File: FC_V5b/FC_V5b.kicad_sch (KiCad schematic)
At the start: 78 parts, among them IC2 AZ1117CH-3.3TRG1, IC3 RV-3028-C7_32.768kHz_1ppm_TA_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, J1 Conn_01x02, J12 USB_C_Receptacle_USB2.0_16P, J16 DEBUG, J22 SWD Port, J3 Life Makes Lemonade, J4 Molex 503398-1892, J5 BM04B-SRSS-TB(LF)(SN), J6 Conn_Coaxial, J9 BM04B-SRSS-TB(LF)(SN), SW1 KMR2, SW2 KMR2, SW3 SW_Push_SPDT, U12 TCA9548ARGERQ1, U16 MCP9808T-E/MS, U30 E28-2G4M27S, U4 RFM98PW, U5 RFM9xBreakout, U7 LSM6DSOTR, U8 LSM303AGRTR

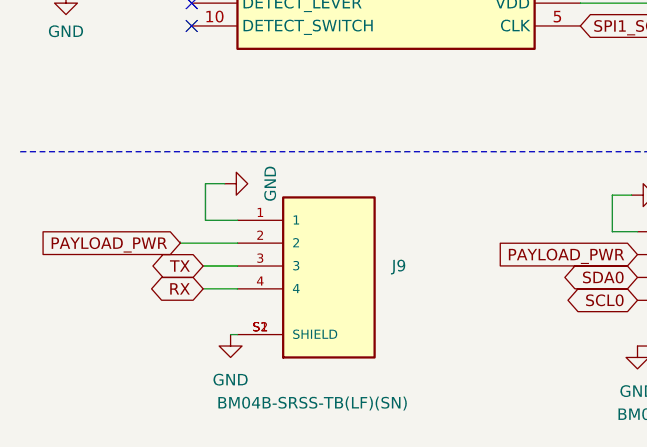
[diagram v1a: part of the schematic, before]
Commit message: Removed UART STEMMA
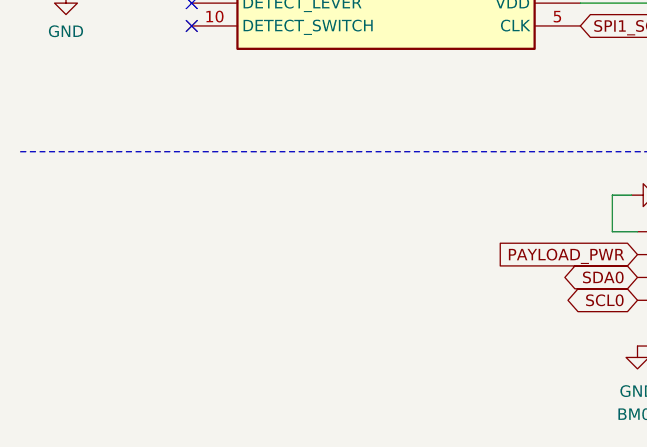
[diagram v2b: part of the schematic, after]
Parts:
- removed J9: BM04B-SRSS-TB(LF)(SN), FC_DEV_BOARD:JST_BM04B-SRSS-TB(LF)(SN), symbol BM04B-SRSS-TB_LF__SN_:BM04B-SRSS-TB(LF)(SN)

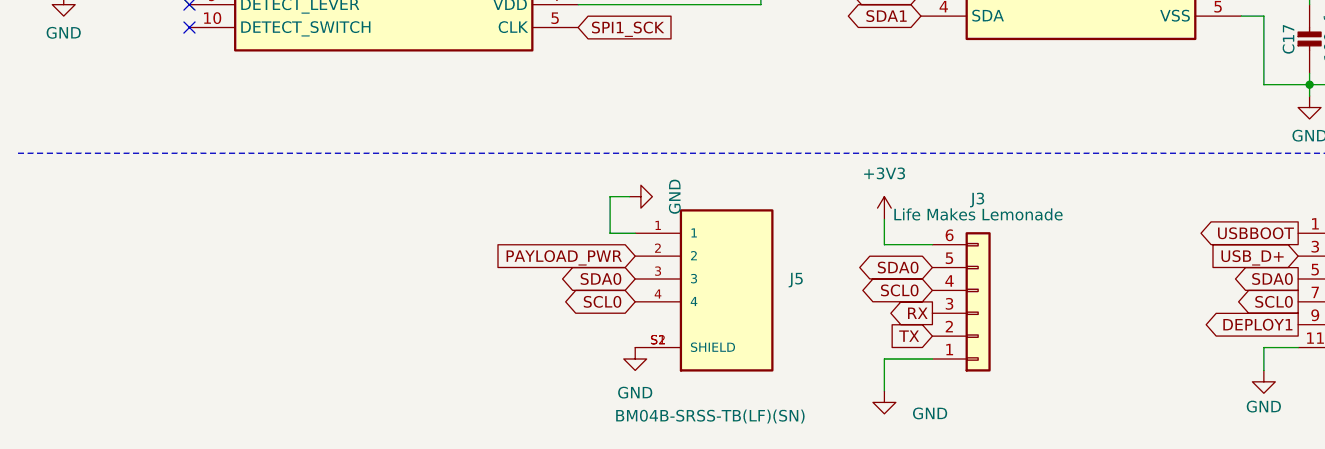
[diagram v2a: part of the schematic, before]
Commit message: Added a 12pos DF11 for Payload Connection
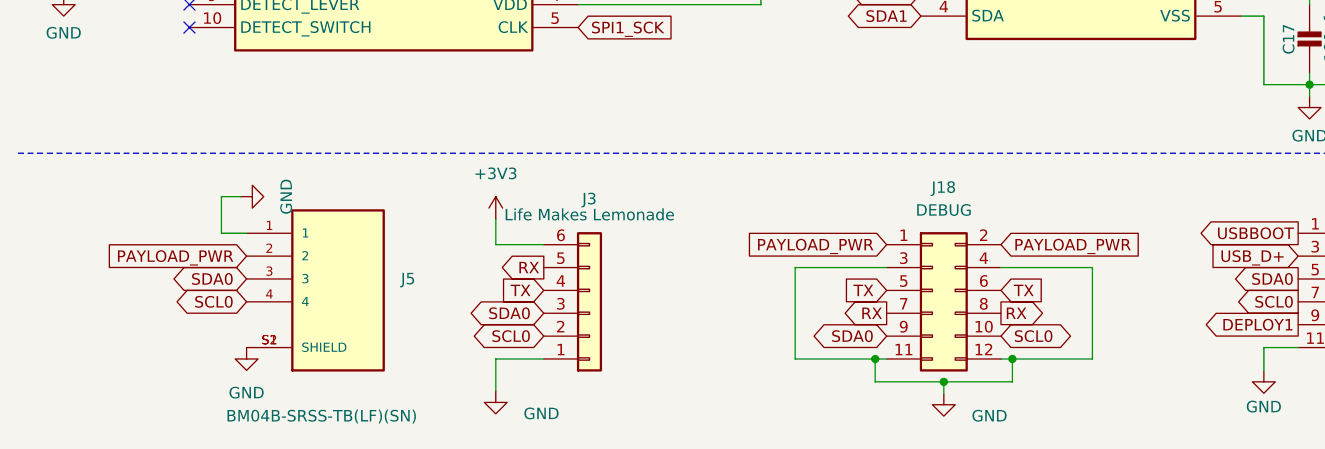
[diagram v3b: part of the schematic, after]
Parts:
- added J18: DEBUG, Connector_Hirose:Hirose_DF11-12DP-2DSA_2x06_P2.00mm_Vertical, symbol Connector_Generic:Conn_02x06_Odd_Even
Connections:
- net GND: now also J18.11 (Pin_11), J18.12 (Pin_12), J18.3 (Pin_3), J18.4 (Pin_4)
- net PAYLOAD_PWR: now also J18.1 (Pin_1), J18.2 (Pin_2)
- net RX: now also J3.5 (Pin_5), J18.7 (Pin_7), J18.8 (Pin_8); no longer J3.3 (Pin_3)
- net SCL0: now also J3.2 (Pin_2), J18.10 (Pin_10); no longer J3.4 (Pin_4)
- net SDA0: now also J3.3 (Pin_3), J18.9 (Pin_9); no longer J3.5 (Pin_5)
- net TX: now also J3.4 (Pin_4), J18.5 (Pin_5), J18.6 (Pin_6); no longer J3.2 (Pin_2)
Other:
- moved on the sheet: J3, J5

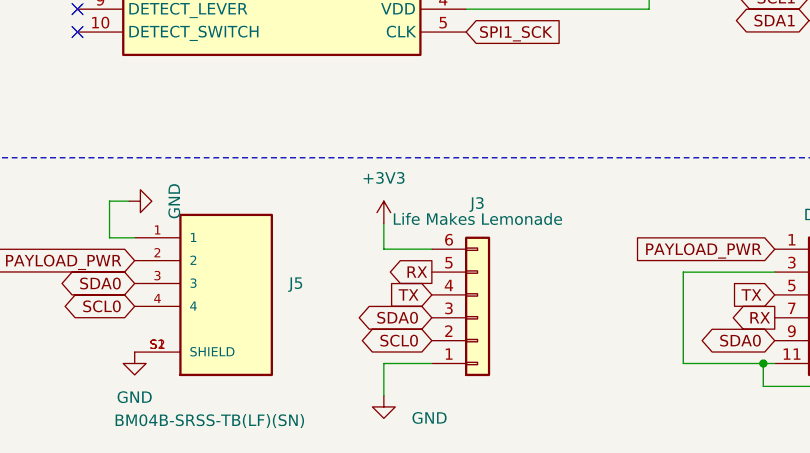
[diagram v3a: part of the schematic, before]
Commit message: Reduced TCA Solder Mask
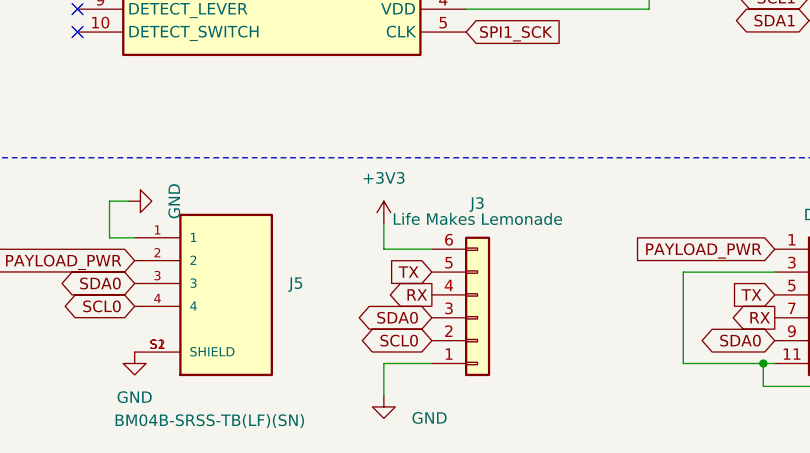
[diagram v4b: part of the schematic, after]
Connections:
- net RX: now also J3.4 (Pin_4); no longer J3.5 (Pin_5)
- net TX: now also J3.5 (Pin_5); no longer J3.4 (Pin_4)

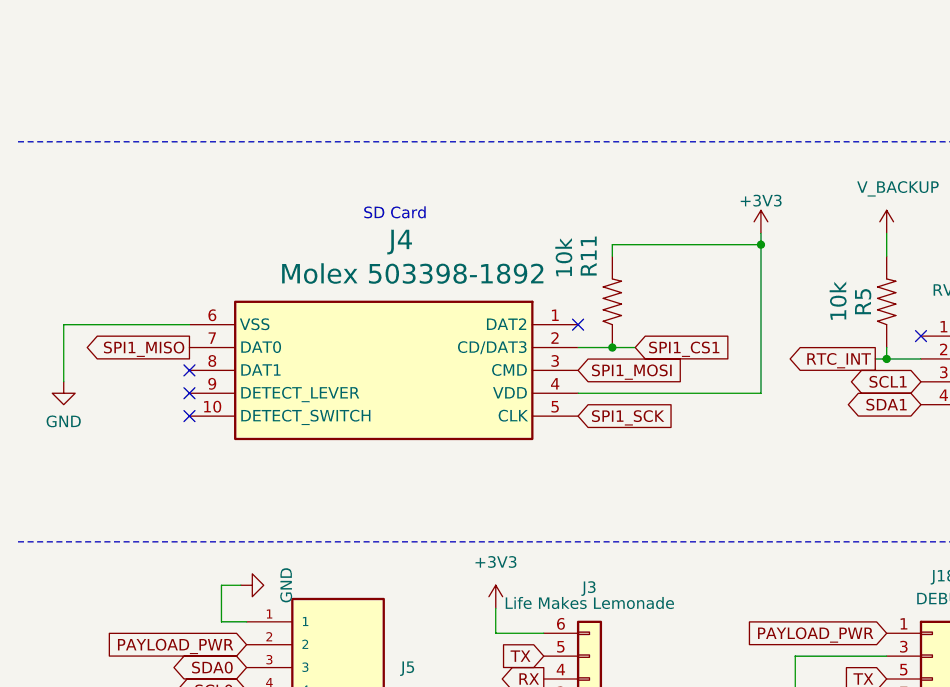
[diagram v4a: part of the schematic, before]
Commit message: Replaced SD Card Slot with ZSD NAND Chip
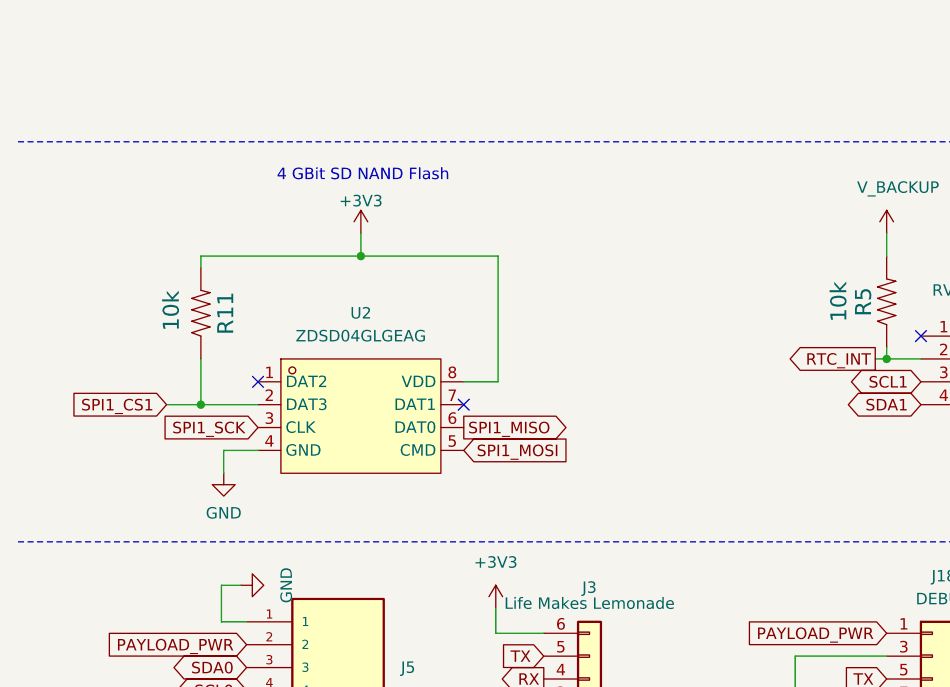
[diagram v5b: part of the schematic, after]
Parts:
- removed J4: Molex 503398-1892, 503398-1892-1, symbol Molex 503398-1892:503398-1892
- added U2: ZDSD04GLGEAG, easyeda2kicad:LGA-8_L8.0-W6.0-P1.27-TL-1, symbol easyeda2kicad:ZDSD04GLGEAG
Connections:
- net +3V3: now also U2.8 (VDD)
- net GND: now also U2.4 (GND)
- net SPI1_CS1: now also U2.2 (DAT3)
- net SPI1_MISO: now also U2.6 (DAT0)
- net SPI1_MOSI: now also U2.5 (CMD)
- net SPI1_SCK: now also U2.3 (CLK)
- no-connect marks 33 -> 31
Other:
- note added: "4 GBit SD NAND Flash"
- note removed: "SD Card"
- moved on the sheet: R11

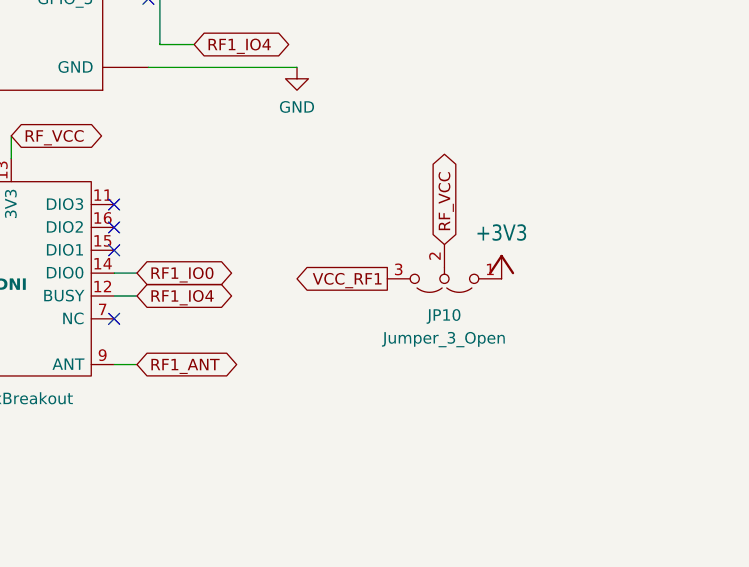
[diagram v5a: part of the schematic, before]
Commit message: Removed Unusued RF Power Selector
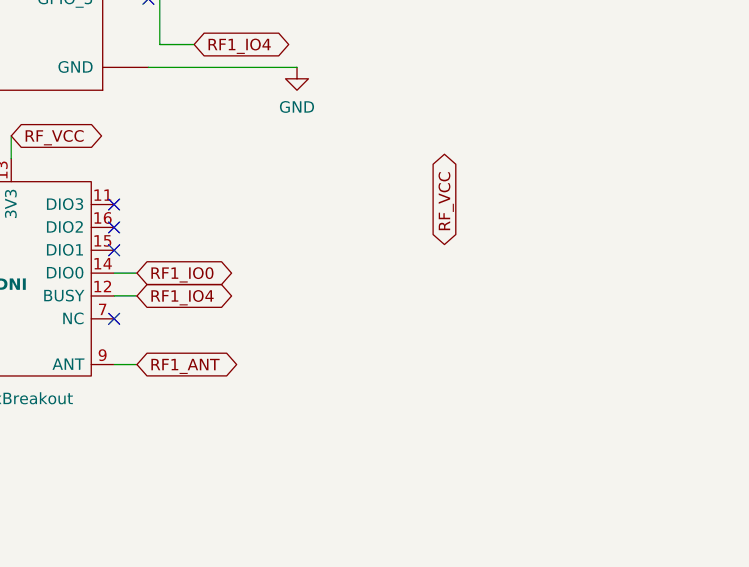
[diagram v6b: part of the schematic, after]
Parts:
- removed JP10: Jumper_3_Open, Jumper:SolderJumper-3_P1.3mm_Open_RoundedPad1.0x1.5mm_NumberLabels, symbol Jumper:Jumper_3_Open
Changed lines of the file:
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@@
 		)
 	)
-	(global_label "VCC_RF1"
-		(shape output)
-		(at 380.873 236.855 180)
-		(fields_autoplaced yes)
-		(effects
-			(font
-				(size 1.27 1.27)
-			)
-			(justify right)
-		)
-		(property "Intersheetrefs" "${INTERSHEET_REFS}"
-			(at 369.8029 236.855 0)
-			(effects
-				(font
-					(size 1.27 1.27)
-				)
-				(justify right)
-				(hide yes)
-			)
-		)
-	)
 	(symbol
 		(lib_id "mainboard:RESISTOR0603")
@@
 	)
 	(symbol
-		(lib_id "Adafruit ItsyBitsy RP2040-eagle-import:+3V3")
-		(at 393.573 234.315 0)
-		(unit 1)
-		(exclude_from_sim no)
-		(in_bom yes)
-		(on_board yes)
-		(dnp no)
-		(fields_autoplaced yes)
-		(property "Reference" "#+3V016"
-			(at 393.573 234.315 0)
-			(effects
-				(font
-					(size 1.27 1.27)
-				)
-				(hide yes)
-			)
-		)
-		(property "Value" "+3V3"
-			(at 393.573 231.775 0)
-			(effects
-				(font
-					(size 1.778 1.5113)
-				)
-			)
-		)
-		(property "Footprint" "Adafruit ItsyBitsy RP2040:"
-			(at 393.573 234.315 0)
-			(effects
-				(font
-					(size 1.27 1.27)
-				)
-				(hide yes)
-			)
-		)
-		(property "Datasheet" ""
-			(at 393.573 234.315 0)
-			(effects
-				(font
-					(size 1.27 1.27)
-				)
-				(hide yes)
-			)
-		)
-		(property "Description" ""
-			(at 393.573 234.315 0)
-			(effects
-				(font
-					(size 1.27 1.27)
-				)
-				(hide yes)
-			)
-		)
-		(pin "1"
-		)
-		(instances
-			(project "FC_V5"
-				(path "/c64c0d72-a9f6-4f3a-891e-1f647558f538"
-					(reference "#+3V016")
-					(unit 1)
-				)
-			)
-		)
-	)
-	(symbol
 		(lib_id "Connector_Generic:Conn_01x06")
 		(at 74.93 271.78 0)
@@
 					(unit 1)
 				)
-			)
-		)
-	)
-	(symbol
-		(lib_id "Jumper:Jumper_3_Open")
-		(at 387.223 236.855 180)
-		(unit 1)
-		(exclude_from_sim no)
-		(in_bom yes)
-		(on_board yes)
-		(dnp no)
-		(fields_autoplaced yes)
-		(property "Reference" "JP10"
-			(at 387.223 240.919 0)
-			(effects
-				(font
-					(size 1.27 1.27)
-				)
-			)
-		)
-		(property "Value" "Jumper_3_Open"
-			(at 387.223 243.459 0)
-			(effects
-				(font
-					(size 1.27 1.27)
-				)
-			)
-		)
-		(property "Footprint" "Jumper:SolderJumper-3_P1.3mm_Open_RoundedPad1.0x1.5mm_NumberLabels"
-			(at 387.223 236.855 0)
-			(effects
-				(font
-					(size 1.27 1.27)
-				)
-				(hide yes)
-			)
-		)
-		(property "Datasheet" "~"
-			(at 387.223 236.855 0)
-			(effects
-				(font
-					(size 1.27 1.27)
-				)
-				(hide yes)
-			)
-		)
-		(property "Description" ""
-			(at 387.223 236.855 0)
-			(effects
-				(font
-					(size 1.27 1.27)
-				)
-				(hide yes)
-			)
-		)
-		(pin "1"
-		)
-		(pin "2"
-		)
-		(pin "3"
-		)
-		(instances
-			(project "FC_V5"
-				(path "/c64c0d72-a9f6-4f3a-891e-1f647558f538"
-					(reference "JP10")
-					(unit 1)
-				)

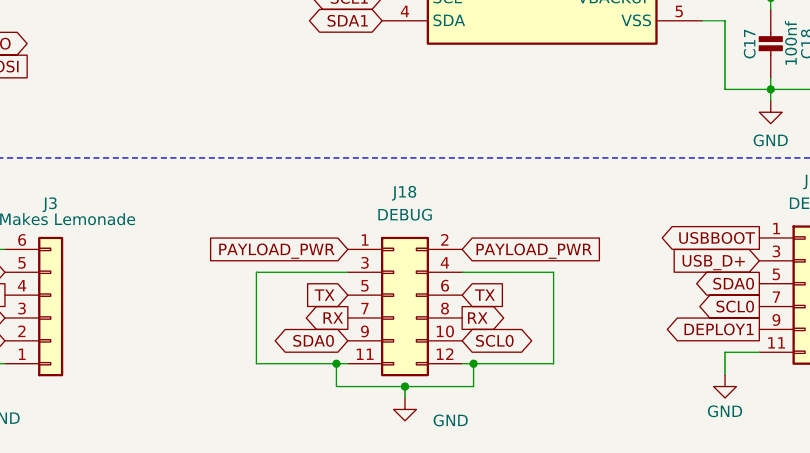
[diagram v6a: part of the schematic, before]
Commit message: Repositioned Sys INA and Removed VBUSP TP
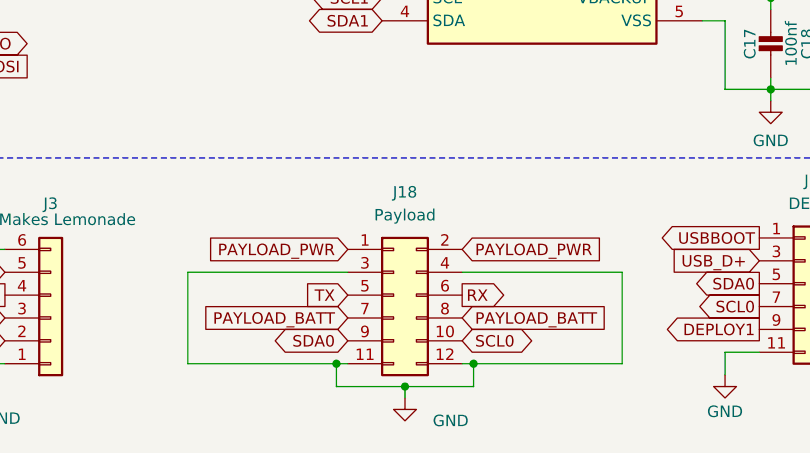
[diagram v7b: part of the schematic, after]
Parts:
- J18: value DEBUG -> Payload
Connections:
- net RX: now also J18.6 (Pin_6); no longer J18.7 (Pin_7), J18.8 (Pin_8)
- net TX: no longer J18.6 (Pin_6)
- new net PAYLOAD_BATT: J18.7 (Pin_7), J18.8 (Pin_8)
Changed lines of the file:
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@@
 	(wire
 		(pts
-			(xy 120.65 266.7) (xy 130.81 266.7)
+			(xy 120.65 266.7) (xy 138.43 266.7)
 		)
 		(stroke
@@
 	(wire
 		(pts
-			(xy 97.79 276.86) (xy 106.68 276.86)
+			(xy 90.17 276.86) (xy 106.68 276.86)
 		)
 		(stroke
@@
 	(wire
 		(pts
-			(xy 130.81 276.86) (xy 121.92 276.86)
+			(xy 138.43 276.86) (xy 121.92 276.86)
 		)
 		(stroke
@@
 	(wire
 		(pts
-			(xy 97.79 266.7) (xy 97.79 276.86)
+			(xy 90.17 266.7) (xy 90.17 276.86)
 		)
 		(stroke
@@
 	(wire
 		(pts
-			(xy 107.95 266.7) (xy 97.79 266.7)
+			(xy 107.95 266.7) (xy 90.17 266.7)
 		)
 		(stroke
@@
 	(wire
 		(pts
-			(xy 130.81 266.7) (xy 130.81 276.86)
+			(xy 138.43 266.7) (xy 138.43 276.86)
 		)
 		(stroke
@@
 		)
 	)
+	(global_label "PAYLOAD_BATT"
+		(shape input)
+		(at 120.65 271.78 0)
+		(fields_autoplaced yes)
+		(effects
+			(font
+				(size 1.27 1.27)
+			)
+			(justify left)
+		)
+		(property "Intersheetrefs" "${INTERSHEET_REFS}"
+			(at 137.061 271.78 0)
+			(effects
+				(font
+					(size 1.27 1.27)
+				)
+				(justify left)
+				(hide yes)
+			)
+		)
+	)
 	(global_label "RF1_IO4"
 		(shape bidirectional)
@@
 		)
 	)
+	(global_label "RX"
+		(shape output)
+		(at 120.65 269.24 0)
+		(fields_autoplaced yes)
+		(effects
+			(font
+				(size 1.27 1.27)
+			)
+			(justify left)
+		)
+		(property "Intersheetrefs" "${INTERSHEET_REFS}"
+			(at 126.1147 269.24 0)
+			(effects
+				(font
+					(size 1.27 1.27)
+				)
+				(justify left)
+				(hide yes)
+			)
+		)
+	)
 	(global_label "USBBOOT"
 		(shape output)
@@
 		)
 	)
-	(global_label "TX"
-		(shape input)
-		(at 120.65 269.24 0)
-		(fields_autoplaced yes)
-		(effects
-			(font
-				(size 1.27 1.27)
-			)
-			(justify left)
-		)
-		(property "Intersheetrefs" "${INTERSHEET_REFS}"
-			(at 125.8123 269.24 0)
-			(effects
-				(font
-					(size 1.27 1.27)
-				)
-				(justify left)
-				(hide yes)
-			)
-		)
-	)
 	(global_label "SPI0_MISO"
 		(shape output)
@@
 		)
 	)
-	(global_label "RX"
-		(shape output)
-		(at 120.65 271.78 0)
-		(fields_autoplaced yes)
-		(effects
-			(font
-				(size 1.27 1.27)
-			)
-			(justify left)
-		)
-		(property "Intersheetrefs" "${INTERSHEET_REFS}"
-			(at 126.1147 271.78 0)
-			(effects
-				(font
-					(size 1.27 1.27)
-				)
-				(justify left)
-				(hide yes)
-			)
-		)
-	)
 	(global_label "SCL0"
 		(shape bidirectional)
@@
 		)
 	)
-	(global_label "SPI1_MISO"
-		(shape output)
-		(at 60.96 241.3 0)
+	(global_label "PAYLOAD_BATT"
+		(shape input)
+		(at 107.95 271.78 180)
 		(fields_autoplaced yes)
 		(effects
@@
 				(size 1.27 1.27)
 			)
-			(justify left)
+			(justify right)
 		)
 		(property "Intersheetrefs" "${INTERSHEET_REFS}"
-			(at 73.8028 241.3 0)
+			(at 91.539 271.78 0)
 			(effects
 				(font
 					(size 1.27 1.27)
 				)
-				(justify left)
+				(justify right)
 				(hide yes)
 			)
 		)
 	)
-	(global_label "F2_SCL"
+	(global_label "SPI1_MISO"
 		(shape output)
-		(at 241.3 115.57 180)
+		(at 60.96 241.3 0)
 		(fields_autoplaced yes)
 		(effects
@@
 				(size 1.27 1.27)
 			)
-			(justify right)
+			(justify left)
 		)
 		(property "Intersheetrefs" "${INTERSHEET_REFS}"
-			(at 232.1136 115.4906 0)
+			(at 73.8028 241.3 0)
 			(effects
 				(font
 					(size 1.27 1.27)
 				)
-				(justify right)
+				(justify left)
 				(hide yes)
 			)
 		)
 	)
-	(global_label "RX"
+	(global_label "F2_SCL"
 		(shape output)
-		(at 107.95 271.78 180)
+		(at 241.3 115.57 180)
 		(fields_autoplaced yes)
 		(effects
@@
 		)
 		(property "Intersheetrefs" "${INTERSHEET_REFS}"
-			(at 103.0574 271.7006 0)
+			(at 232.1136 115.4906 0)
 			(effects
 				(font
@@
 			)
 		)
-		(property "Value" "DEBUG"
+		(property "Value" "Payload"
 			(at 114.3 260.35 0)
 			(effects

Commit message: Squashing DRC Errors
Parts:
- R7, R8: footprint Resistor_SMD:R_0603_1608Metric -> Resistor_SMD:R_0402_1005Metric
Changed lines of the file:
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@@
 			)
 		)
-		(property "Footprint" "Resistor_SMD:R_0603_1608Metric"
+		(property "Footprint" "Resistor_SMD:R_0402_1005Metric"
 			(at 186.69 38.1 0)
 			(effects
@@
 			)
 		)
-		(property "Description" "100K 0603"
+		(property "Description" "USB Termination Resistor"
 			(at 186.69 42.164 0)
 			(effects
@@
 			)
 		)
-		(property "Footprint" "Resistor_SMD:R_0603_1608Metric"
+		(property "Footprint" "Resistor_SMD:R_0402_1005Metric"
 			(at 186.69 40.64 0)
 			(effects
@@
 			)
 		)
-		(property "Description" "100K 0603"
+		(property "Description" "USB Termination Resistor"
 			(at 186.69 44.704 0)
 			(effects
